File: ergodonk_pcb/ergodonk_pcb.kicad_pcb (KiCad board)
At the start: 2 copper layers, 184 x 152.6 mm, 124 parts, among them J1 AudioJack4, J2 ICSP, Q1 TIP120, U1 ProMicro, U1 ProMicro-18mil-offset, U1 Solenoid

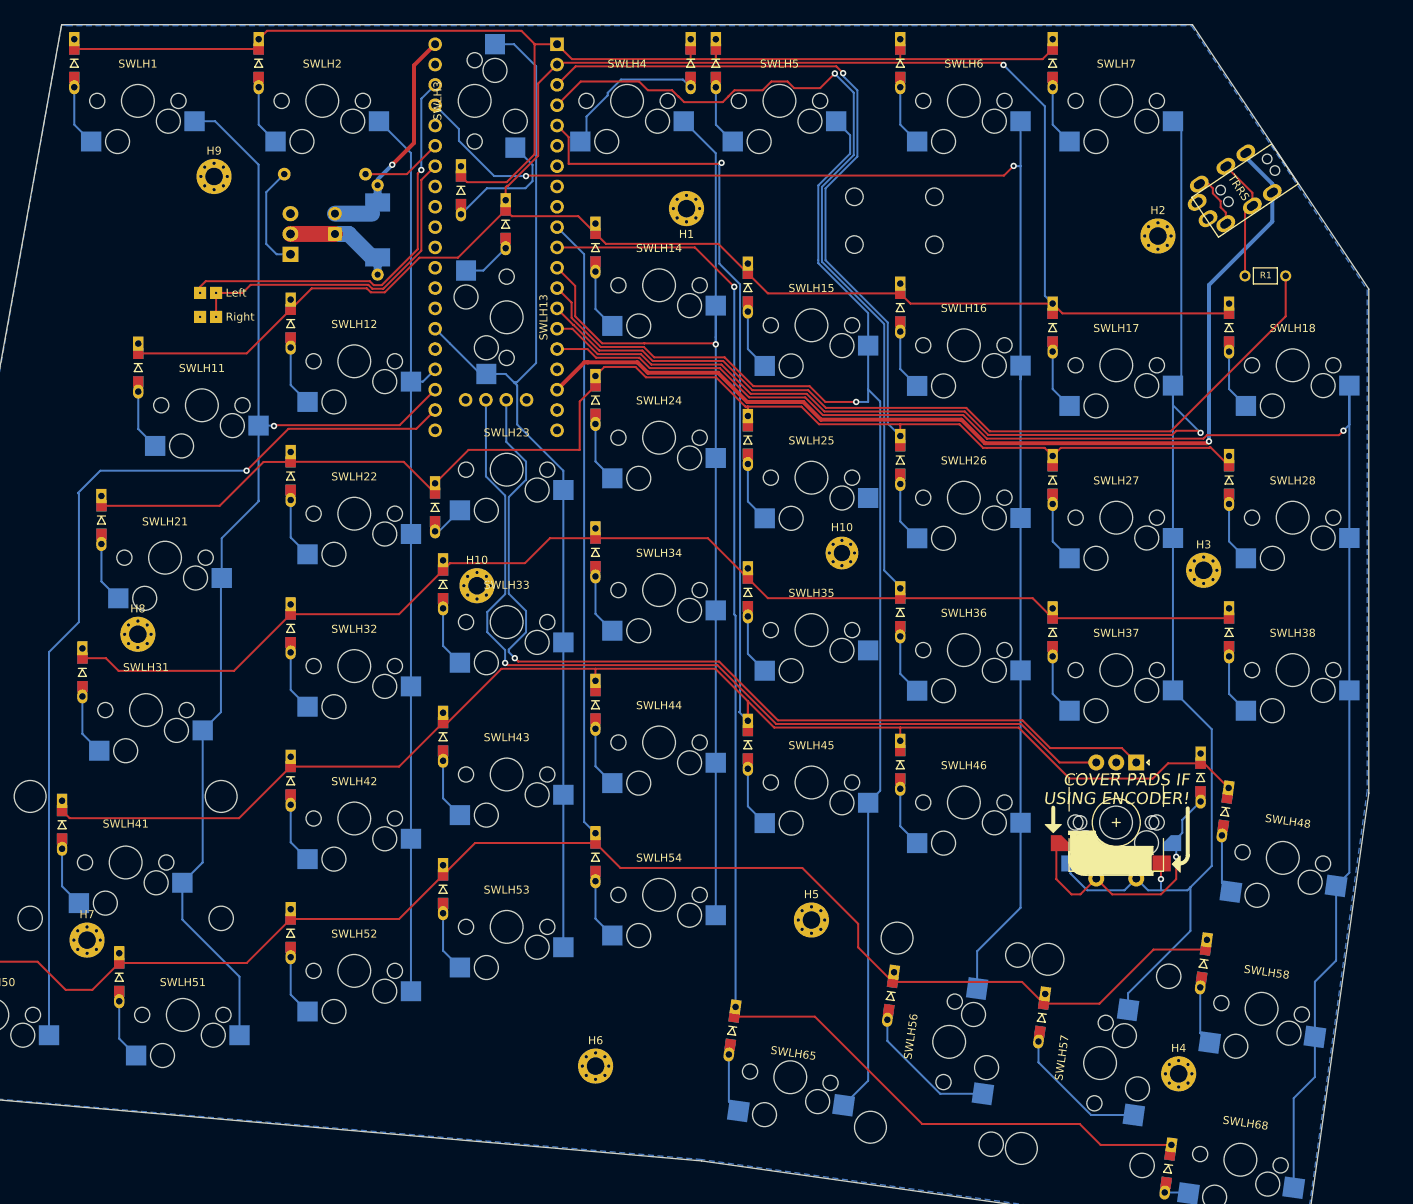
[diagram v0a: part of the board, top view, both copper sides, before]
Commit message: Updated wiring on pcb to v2, ran DRC
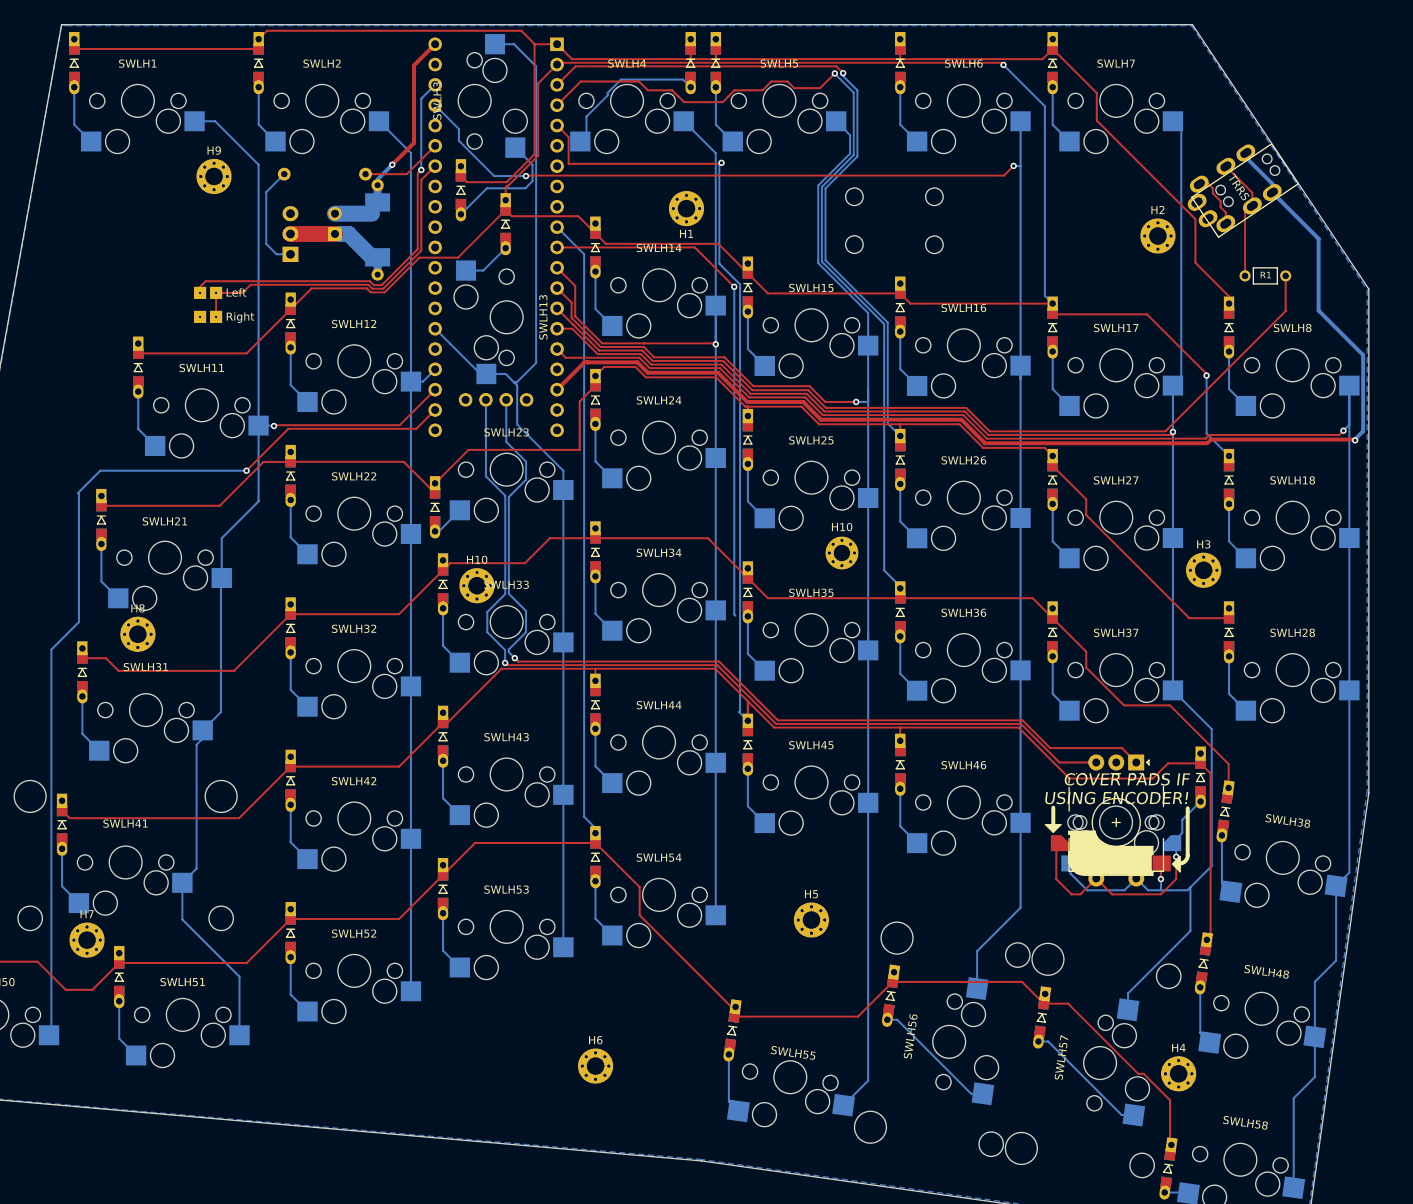
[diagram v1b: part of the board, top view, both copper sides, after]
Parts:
- renumbered D28 to D18, D38 to D28, D48 to D38, D58 to D48, D65 to D55, D68 to D58, D18 to D8, SWLH28 to SWLH18, SWLH38 to SWLH28, SWLH48 to SWLH38, SWLH58 to SWLH48, SWLH65 to SWLH55, SWLH68 to SWLH58, SWLH18 to SWLH8
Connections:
- D18 pad 1: row2 -> row1
- D28 pad 1: row3 -> row2
- D38 pad 1: row4 -> row3
- D48 pad 1: row5 -> row4
- D55 pad 1: row6 -> row5
- D58 pad 1: row6 -> row5
- D8 pad 1: row1 -> row0
- ULH1 pad 11: row6 -> unconnected-(ULH1-Pad11)
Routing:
- net row6: track 175.6 -> 0.00 mm, vias 1 -> 0
- net unconnected-(ULH1-Pad11): track 0.00 -> 65.4 mm, vias 0 -> 1
- net row0: track 154.5 -> 196.7 mm
- net TRRS_VCC: track 127.9 -> 148.1 mm
- net row4: track 270.6 -> 289.2 mm
- net row3: track 265.3 -> 276.9 mm
- net row1: track 257.6 -> 268.9 mm, vias 1 -> 2
- net row5: track 259.3 -> 270.1 mm
- net SW47A: track 233.8 -> 225.4 mm
- net row2: track 258.6 -> 266.2 mm
- net Net-(D56-Pad2): track 17.3 -> 15.8 mm
- net Net-(D57-Pad2): track 17.3 -> 15.7 mm
- net Net-(D54-Pad2): track 7.66 -> 8.89 mm
- net col5: track 177.9 -> 178.8 mm

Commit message: Revised RH wiring diagram and added 3d component models
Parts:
- moved U1 68.7 mm to (216.1, 96.2)
- moved REF** 14.3 mm to (239.8, 61.0)

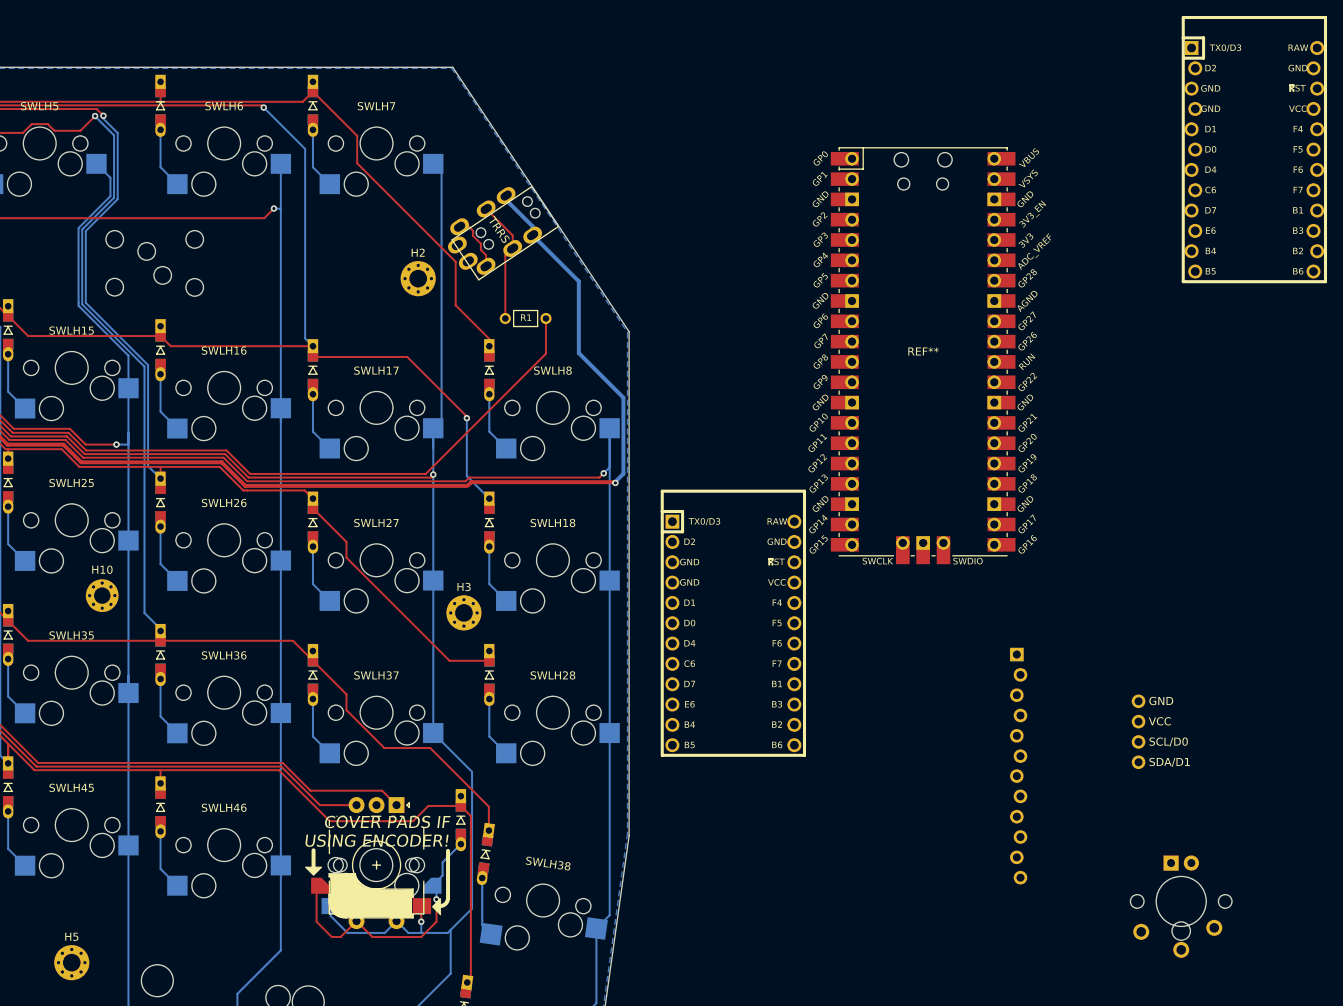
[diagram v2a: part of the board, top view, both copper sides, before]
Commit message: Added KiCad libraries for rp2040 pro micro and Sofle Choc
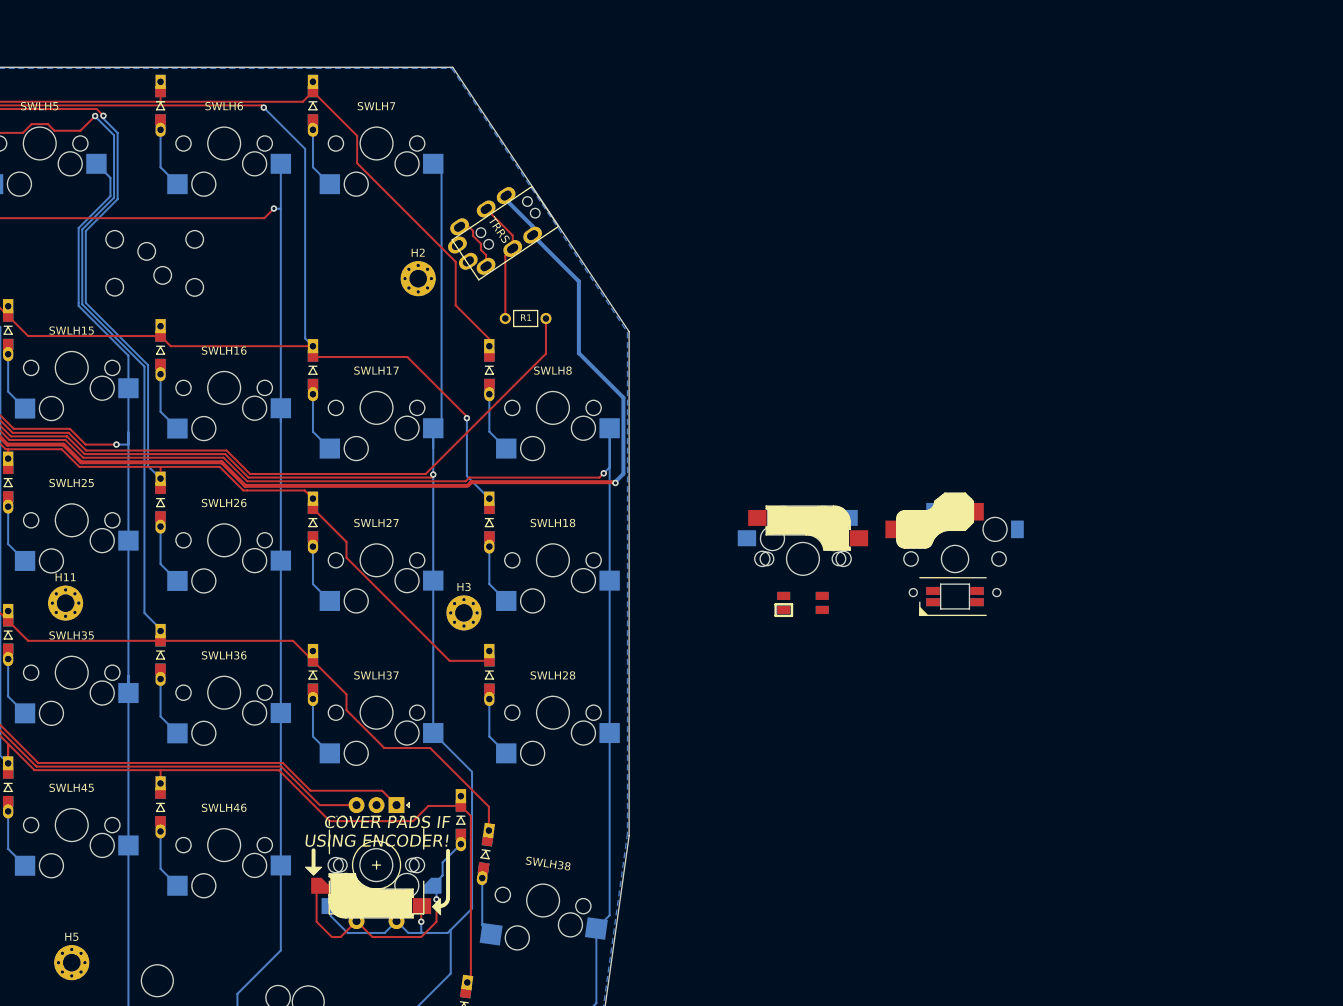
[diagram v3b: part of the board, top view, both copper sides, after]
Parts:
- removed the H10 at (137.2, 91.4)
- removed J2: ICSP, Keebio-Parts:Header-12-Pin-ZigZag-Square
- removed Low Profile Hybrid: MXLP/Choc, Keebio-Parts:Low-Profile-Choc-MX
- removed REF*: I2C_Breakout, Keebio-Parts:I2C_Breakout
- removed REF**: RPi_Pico_SMD_TH, MCU_RaspberryPi_and_Boards:RPi_Pico_SMD_TH
- removed U1: ProMicro-18mil-offset, Keebio-Parts:ArduinoProMicro-ZigZag
- removed U1: ProMicro, Keebio-Parts:ArduinoProMicro
- added H11: MountingHole, MountingHole:MountingHole_2.2mm_M2_Pad_Via, F.Cu at (132.6, 92.4)
- added SW1: SW_PUSH-MX_W_LED, SofleChoc:SK6812MINI_and_cherry, F.Cu at (224.8, 86.8)
- added SW4: SW_PUSH, SofleChoc:Choc_Hotswap_SK6812MiniE, F.Cu at (243.8, 86.9)
- renumbered U1 to S1
